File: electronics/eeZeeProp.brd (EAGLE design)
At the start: 47.2 x 23.9 mm, 34 parts, among them Q1 5MHz, Q2 2N3904SOT23, SW1 RESET, U1 P8X32A-Q44, U2 24LC256-I/ST, U3 NCP1117 3V3

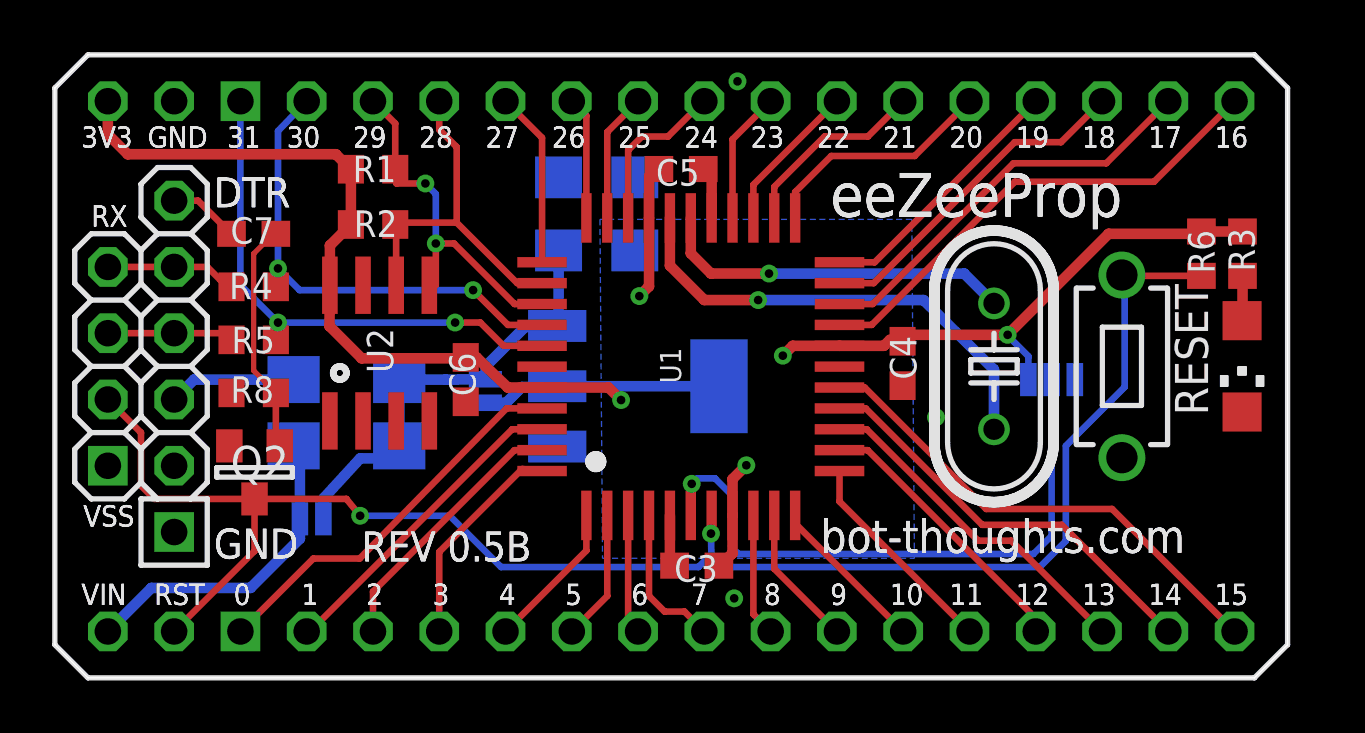
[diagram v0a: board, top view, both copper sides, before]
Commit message: Revised silkscreen labels, added user guide link, minor relocation of 3v3 ftdi solder jumper and label, updated bt logo
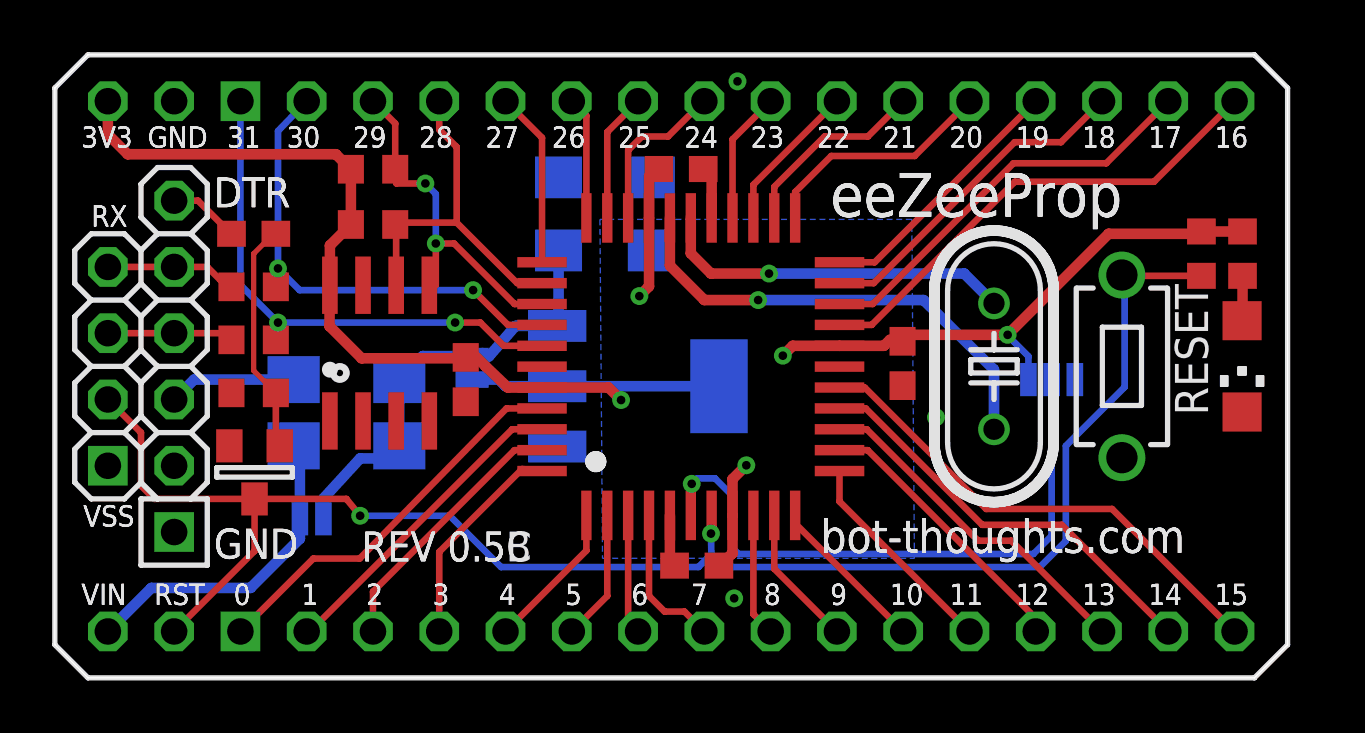
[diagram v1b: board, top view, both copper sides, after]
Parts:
- added U$1: BTLOGO-LOGO-MD, bt:BTLOGOM
- moved SJ3 1.02 mm to (16.0, 11.9)
- moved C2 0.63 mm to (22.9, 17.8)
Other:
- board text added: "CC-BY-SA"
- board text added: "REV 0.5C"
- board text added: "User Guide: goo.gl/Ydheu7"
- board text added: "VCC"
